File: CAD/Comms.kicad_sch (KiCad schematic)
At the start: 84 parts, among them J27 uSD_Socket, J43 USB, J46 ETHERNET, Q1 BC807, U13 MCP2542, U15 MCP2542, U16 KSZ8081RNACA, U17 74LVC2G125, U19 74LVC2G34, U3 EMIF06, U5 RClamp0504FB, U7 AP22816AKEWT, X2 25Mhz

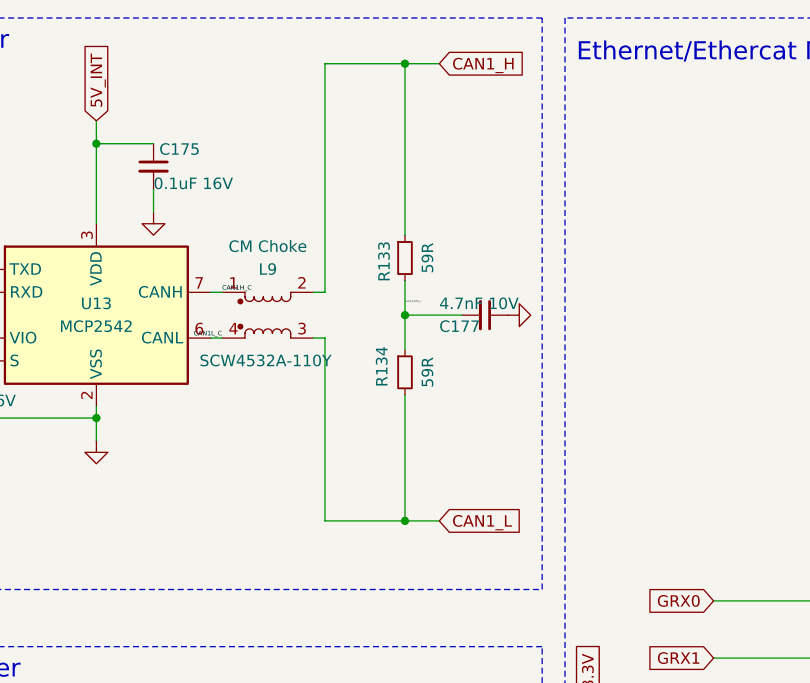
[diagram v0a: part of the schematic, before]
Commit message: OOPS, switched the symbols for psoitive and negative
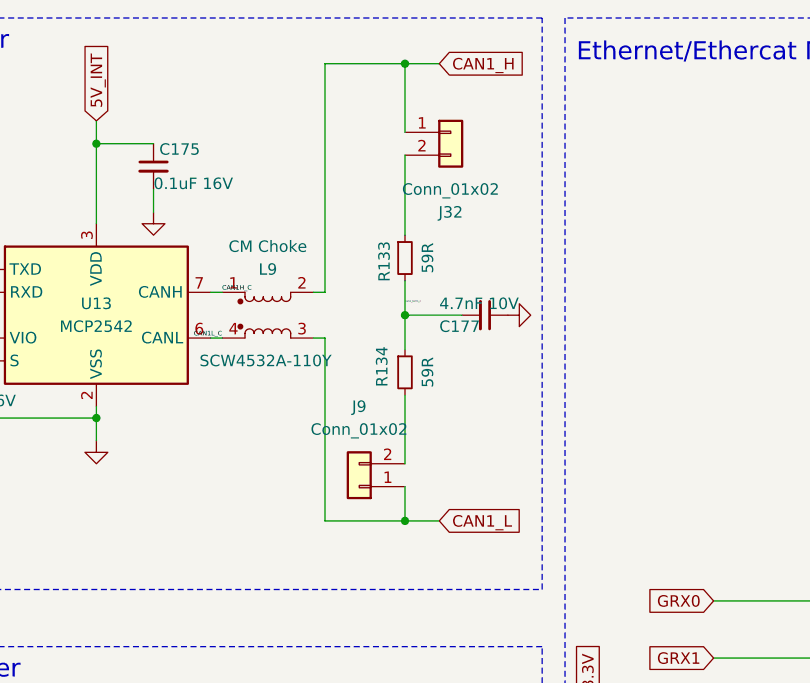
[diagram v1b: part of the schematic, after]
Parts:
- added J32, J9: Conn_01x02, Connector_PinHeader_2.54mm:PinHeader_1x02_P2.54mm_Vertical, symbol Connector_Generic:Conn_01x02
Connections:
- net CAN1_H: now also J32.1 (Pin_1); no longer R133.1
- net CAN1_L: now also J9.1 (Pin_1); no longer R134.2
- new net: J32.2 (Pin_2), R133.1
- new net: J9.2 (Pin_2), R134.2
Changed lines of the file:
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@@
 	(wire
 		(pts
+			(xy 86.36 67.31) (xy 86.36 71.12)
+		)
+		(stroke
+			(width 0)
+			(type default)
+		)
+	)
+	(wire
+		(pts
 			(xy 76.2 257.81) (xy 77.47 257.81)
 		)
@@
 	(wire
 		(pts
-			(xy 86.36 57.15) (xy 86.36 71.12)
+			(xy 86.36 57.15) (xy 86.36 64.77)
 		)
 		(stroke
@@
 	(wire
 		(pts
-			(xy 86.36 20.32) (xy 86.36 39.37)
+			(xy 86.36 20.32) (xy 86.36 27.94)
 		)
 		(stroke
@@
 	(wire
 		(pts
+			(xy 86.36 30.48) (xy 86.36 39.37)
+		)
+		(stroke
+			(width 0)
+			(type default)
+		)
+	)
+	(wire
+		(pts
 			(xy 90.17 170.18) (xy 93.98 170.18)
 		)
@@
 	)
 	(symbol
+		(lib_id "Connector_Generic:Conn_01x02")
+		(at 91.44 27.94 0)
+		(unit 1)
+		(exclude_from_sim no)
+		(in_bom yes)
+		(on_board yes)
+		(dnp no)
+		(fields_autoplaced yes)
+		(property "Reference" "J32"
+			(at 91.44 36.83 0)
+			(effects
+				(font
+					(size 1.27 1.27)
+				)
+			)
+		)
+		(property "Value" "Conn_01x02"
+			(at 91.44 34.29 0)
+			(effects
+				(font
+					(size 1.27 1.27)
+				)
+			)
+		)
+		(property "Footprint" "Connector_PinHeader_2.54mm:PinHeader_1x02_P2.54mm_Vertical"
+			(at 91.44 27.94 0)
+			(effects
+				(font
+					(size 1.27 1.27)
+				)
+				(hide yes)
+			)
+		)
+		(property "Datasheet" "~"
+			(at 91.44 27.94 0)
+			(effects
+				(font
+					(size 1.27 1.27)
+				)
+				(hide yes)
+			)
+		)
+		(property "Description" "Generic connector, single row, 01x02, script generated (kicad-library-utils/schlib/autogen/connector/)"
+			(at 91.44 27.94 0)
+			(effects
+				(font
+					(size 1.27 1.27)
+				)
+				(hide yes)
+			)
+		)
+		(property "LCSC" "C124375"
+			(at 91.44 27.94 0)
+			(effects
+				(font
+					(size 1.524 1.524)
+				)
+				(hide yes)
+			)
+		)
+		(property "RotOffset" "90"
+			(at 91.44 27.94 0)
+			(effects
+				(font
+					(size 1.524 1.524)
+				)
+				(hide yes)
+			)
+		)
+		(pin "1"
+		)
+		(pin "2"
+		)
+		(instances
+			(project "Duet3_MB_3DP"
+				(path "/94813053-1316-4754-9fb4-4dbbf7dc780d/00000000-0000-0000-0000-00005b64a4e7"
+					(reference "J32")
+					(unit 1)
+				)
+			)
+		)
+	)
+	(symbol
 		(lib_id "Device:R_Small")
 		(at 175.26 204.47 0)
@@
 					(unit 1)
 				)
+			)
+		)
+	)
+	(symbol
+		(lib_id "Connector_Generic:Conn_01x02")
+		(at 81.28 67.31 180)
+		(unit 1)
+		(exclude_from_sim no)
+		(in_bom yes)
+		(on_board yes)
+		(dnp no)
+		(fields_autoplaced yes)
+		(property "Reference" "J9"
+			(at 81.28 58.42 0)
+			(effects
+				(font
+					(size 1.27 1.27)
+				)
+			)
+		)
+		(property "Value" "Conn_01x02"
+			(at 81.28 60.96 0)
+			(effects
+				(font
+					(size 1.27 1.27)
+				)
+			)
+		)
+		(property "Footprint" "Connector_PinHeader_2.54mm:PinHeader_1x02_P2.54mm_Vertical"
+			(at 81.28 67.31 0)
+			(effects
+				(font
+					(size 1.27 1.27)
+				)
+				(hide yes)
+			)
+		)
+		(property "Datasheet" "~"
+			(at 81.28 67.31 0)
+			(effects
+				(font
+					(size 1.27 1.27)
+				)
+				(hide yes)
+			)
+		)
+		(property "Description" "Generic connector, single row, 01x02, script generated (kicad-library-utils/schlib/autogen/connector/)"
+			(at 81.28 67.31 0)
+			(effects
+				(font
+					(size 1.27 1.27)
+				)
+				(hide yes)
+			)
+		)
+		(property "LCSC" "C124375"
+			(at 81.28 67.31 0)
+			(effects
+				(font
+					(size 1.524 1.524)
+				)
+				(hide yes)
+			)
+		)
+		(property "RotOffset" "90"
+			(at 81.28 67.31 0)
+			(effects
+				(font
+					(size 1.524 1.524)
+				)
+				(hide yes)
+			)
+		)
+		(pin "1"
+		)
+		(pin "2"
+		)
+		(instances
+			(project "Duet3_MB_3DP"
+				(path "/94813053-1316-4754-9fb4-4dbbf7dc780d/00000000-0000-0000-0000-00005b64a4e7"
+					(reference "J9")
+					(unit 1)
+				)

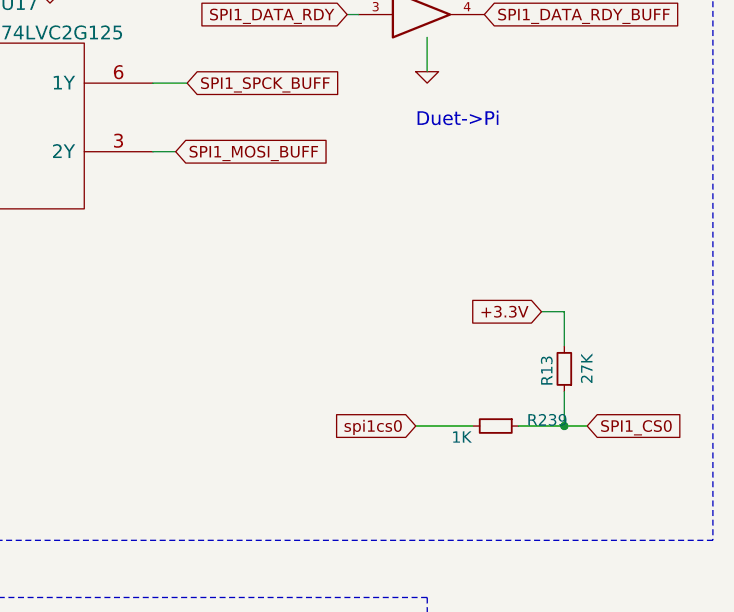
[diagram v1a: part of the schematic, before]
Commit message: Pin Changes / Misc
Changing some pins around so I have a chip select
Processor Pins:
PC28 ---> PA9 (Driver_2_Step)
PC29[AFE1_AD4] ---> PB1[AFE1_AD0] (TEMP_1)
PC28 -> spi1cs1
PC29 -> spi1cs2 (Unused as of now)
IDC Header:
CAN 0 Lines removed
13 -> SPI1_MOSI_BUFF
14 -> SP1_MISO
18 -> SPI1_SPCK_BUFF
19 -> spi1cs1
Misc:
Fixed all library links, should get a lot less errors now
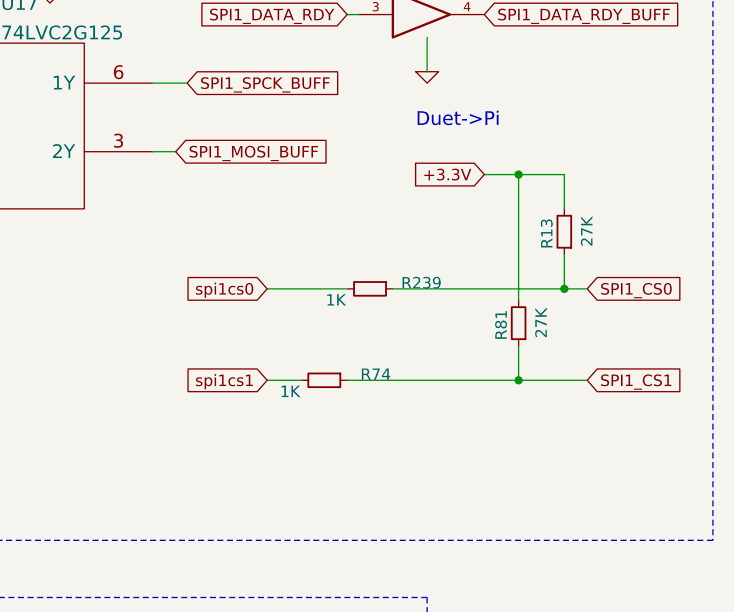
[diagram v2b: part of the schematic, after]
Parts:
- added R74: 1K, Resistor_SMD:R_0402_1005Metric, symbol Device:R_Small
- added R81: 27K, Resistor_SMD:R_0402_1005Metric, symbol Device:R_Small
- C14, C15, C171, C174, C175, C177, C181, C183, C188, C191, C192, C193, C194, C227: footprint Capacitor_SMD:C_0402_1005Metric_Wbry -> Capacitor_SMD:C_0402_1005Metric
- C184: footprint Capacitor_SMD:C_0603_1608Metric_Wbry -> Capacitor_SMD:C_0603_1608Metric
- L10: footprint Resistor_SMD:R_0603_1608Metric_Wbry -> Resistor_SMD:R_0603_1608Metric
- L9: footprint Carters_Various_Bits_and_Pieces:LineKey_CM_Choke_SCW_4532A -> 3DPotter:LineKey_CM_Choke_SCW_4532A
- R119, R122, R13, R130, R133, R134, R135, R136, R141, R142, R149, R150, R151, R174, R179, R188, R239, R66, R67, R70, R71, R75, R76, R77, R78, R80, R90: footprint Resistor_SMD:R_0402_1005Metric_Wbry -> Resistor_SMD:R_0402_1005Metric
- U16: footprint Carters_Various_Bits_and_Pieces:KSZ8081RNA _QFN-24-1EP_4x4mm_P0.5mm_EP2.6x2.6mm -> Package_DFN_QFN:QFN-24-1EP_4x4mm_P0.5mm_EP2.6x2.6mm
- U17: footprint Carters_Various_Bits_and_Pieces:X2-DFN2010-8 -> 3DPotter:X2-DFN2010-8
- U5: footprint complib:SC-70-6L -> 3DPotter:SC70_RCLAMP_SEM
- X2: footprint complib:Crystal_SMD_ECS-33B-4Pin_3.2x2.5mm -> Crystal:Crystal_SMD_3225-4Pin_3.2x2.5mm
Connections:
- net +3.3V: now also R81.2
- new net SPI1_CS1: R74.1, R81.1
- new net spi1cs1: R74.2
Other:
- moved on the sheet: R13, R239

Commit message: Board Finished
Board has been slightly modified to add SPI to the BBC.
A lot of library mismatch/ not found errors were fixed. Only errors that exist currently are all related to the silkscreen edges on all 0402 components.
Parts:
- U16: footprint Package_DFN_QFN:QFN-24-1EP_4x4mm_P0.5mm_EP2.6x2.6mm -> 3DPotter:QFN-24-1EP_4x4mm_P0.5mm_EP2.6x2.6mm_THT
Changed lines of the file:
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@@
 			)
 		)
-		(property "Footprint" "Package_DFN_QFN:QFN-24-1EP_4x4mm_P0.5mm_EP2.6x2.6mm"
+		(property "Footprint" "3DPotter:QFN-24-1EP_4x4mm_P0.5mm_EP2.6x2.6mm_THT"
 			(at 180.34 85.09 0)
 			(effects

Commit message: Update Revision 1.56
1.56 Should be production board that is going on all scara* and cartesian printers. 1.56 is a final check that everything is silkscreened properly and all connectors are the correct ones.
*Not all scaras. Only scara that does not have this board should be Jarret Gross' scara
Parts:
- U16: RotOffset 270 -> 180
- U19: RotOffset 270 -> 90
- U3: RotOffset 90 -> 270
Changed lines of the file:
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@@
 			)
 		)
-		(property "RotOffset" "270"
+		(property "RotOffset" "180"
 			(at 180.34 86.36 0)
 			(effects
@@
 			)
 		)
-		(property "RotOffset" "270"
+		(property "RotOffset" "90"
 			(at 251.46 181.61 0)
 			(effects
@@
 			)
 		)
-		(property "RotOffset" "270"
+		(property "RotOffset" "90"
 			(at 251.46 170.18 0)
 			(effects
@@
 			)
 		)
-		(property "RotOffset" "90"
+		(property "RotOffset" "270"
 			(at 69.85 177.8 0)
 			(effects

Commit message: Finalize changes for 1.56
LCSC and P/N updated for excessively out of stock parts.
Silkscreen changes so no more DRC errors
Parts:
- C14, C15, C17, C171, C174, C175, C177, C181, C183, C188, C191, C192, C193, C194, C227: footprint Capacitor_SMD:C_0402_1005Metric -> 3DPotter:0402_1005Metric_NoSilk
- R11, R119, R12, R122, R13, R130, R133, R134, R135, R136, R141, R142, R149, R150, R151, R174, R179, R188, R239, R5, R70, R71, R74, R75, R76, R77, R78, R80, R81, R90: footprint Resistor_SMD:R_0402_1005Metric -> 3DPotter:0402_1005Metric_NoSilk
- R66, R67: footprint Resistor_SMD:R_0402_1005Metric -> 3DPotter:0402_1005Metric_NoSilk; LCSC C226945 -> C2091853; Part Number AC0402FR-0728K7L -> AC0402FR-0728K7L(C226945) Alt CRCW040228K7FKED(C2091853)
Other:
- title: Duet 3 Main Board 3DP -> Duet 3 MB 3DP
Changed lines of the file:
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@@
 	(paper "A3" portrait)
 	(title_block
-		(title "Duet 3 Main Board 3DP")
-		(date "2026-02-17")
-		(rev "1.55")
+		(title "Duet 3 MB 3DP")
+		(date "2026-06-02")
+		(rev "1.56")
 		(company "3DPotter")
 		(comment 1 "(c) 3DPotter")
@@
 			)
 		)
-		(property "Footprint" "Resistor_SMD:R_0402_1005Metric"
+		(property "Footprint" "3DPotter:0402_1005Metric_NoSilk"
 			(at 67.31 220.98 0)
 			(effects
@@
 			)
 		)
-		(property "Footprint" "Resistor_SMD:R_0402_1005Metric"
+		(property "Footprint" "3DPotter:0402_1005Metric_NoSilk"
 			(at 59.69 224.79 0)
 			(effects
@@
 			)
 		)
-		(property "Footprint" "Resistor_SMD:R_0402_1005Metric"
+		(property "Footprint" "3DPotter:0402_1005Metric_NoSilk"
 			(at 48.26 228.6 0)
 			(effects
@@
 			)
 		)
-		(property "Footprint" "Capacitor_SMD:C_0402_1005Metric"
+		(property "Footprint" "3DPotter:0402_1005Metric_NoSilk"
 			(at 52.07 228.6 0)
 			(effects
@@
 			)
 		)
-		(property "Footprint" "Capacitor_SMD:C_0402_1005Metric"
+		(property "Footprint" "3DPotter:0402_1005Metric_NoSilk"
 			(at 58.42 31.75 0)
 			(effects
@@
 			)
 		)
-		(property "Footprint" "Capacitor_SMD:C_0402_1005Metric"
+		(property "Footprint" "3DPotter:0402_1005Metric_NoSilk"
 			(at 34.29 55.88 0)
 			(effects
@@
 			)
 		)
-		(property "Footprint" "Capacitor_SMD:C_0402_1005Metric"
+		(property "Footprint" "3DPotter:0402_1005Metric_NoSilk"
 			(at 95.25 48.26 0)
 			(effects
@@
 			)
 		)
-		(property "Footprint" "Resistor_SMD:R_0402_1005Metric"
+		(property "Footprint" "3DPotter:0402_1005Metric_NoSilk"
 			(at 86.36 41.91 0)
 			(effects
@@
 			)
 		)
-		(property "Footprint" "Resistor_SMD:R_0402_1005Metric"
+		(property "Footprint" "3DPotter:0402_1005Metric_NoSilk"
 			(at 86.36 54.61 0)
 			(effects
@@
 			)
 		)
-		(property "Footprint" "Resistor_SMD:R_0402_1005Metric"
+		(property "Footprint" "3DPotter:0402_1005Metric_NoSilk"
 			(at 128.27 96.52 0)
 			(effects
@@
 			)
 		)
-		(property "Footprint" "Resistor_SMD:R_0402_1005Metric"
+		(property "Footprint" "3DPotter:0402_1005Metric_NoSilk"
 			(at 148.59 73.66 0)
 			(effects
@@
 			)
 		)
-		(property "Footprint" "Resistor_SMD:R_0402_1005Metric"
+		(property "Footprint" "3DPotter:0402_1005Metric_NoSilk"
 			(at 130.81 115.57 0)
 			(effects
@@
 			)
 		)
-		(property "Footprint" "Capacitor_SMD:C_0402_1005Metric"
+		(property "Footprint" "3DPotter:0402_1005Metric_NoSilk"
 			(at 228.6 73.66 0)
 			(effects
@@
 			)
 		)
-		(property "Footprint" "Capacitor_SMD:C_0402_1005Metric"
+		(property "Footprint" "3DPotter:0402_1005Metric_NoSilk"
 			(at 228.6 81.28 0)
 			(effects
@@
 			)
 		)
-		(property "Footprint" "Resistor_SMD:R_0402_1005Metric"
+		(property "Footprint" "3DPotter:0402_1005Metric_NoSilk"
 			(at 222.25 87.63 0)
 			(effects
@@
 			)
 		)
-		(property "Footprint" "Resistor_SMD:R_0402_1005Metric"
+		(property "Footprint" "3DPotter:0402_1005Metric_NoSilk"
 			(at 220.98 92.71 0)
 			(effects
@@
 			)
 		)
-		(property "Footprint" "Resistor_SMD:R_0402_1005Metric"
+		(property "Footprint" "3DPotter:0402_1005Metric_NoSilk"
 			(at 201.93 110.49 0)
 			(effects
@@
 			)
 		)
-		(property "Footprint" "Capacitor_SMD:C_0402_1005Metric"
+		(property "Footprint" "3DPotter:0402_1005Metric_NoSilk"
 			(at 215.9 127 0)
 			(effects
@@
 			)
 		)
-		(property "Footprint" "Capacitor_SMD:C_0402_1005Metric"
+		(property "Footprint" "3DPotter:0402_1005Metric_NoSilk"
 			(at 240.03 127 0)
 			(effects
@@
 			)
 		)
-		(property "Footprint" "Resistor_SMD:R_0402_1005Metric"
+		(property "Footprint" "3DPotter:0402_1005Metric_NoSilk"
 			(at 123.19 100.33 0)
 			(effects
@@
 			)
 		)
-		(property "Footprint" "Resistor_SMD:R_0402_1005Metric"
+		(property "Footprint" "3DPotter:0402_1005Metric_NoSilk"
 			(at 152.4 58.42 0)
 			(effects
@@
 			)
 		)
-		(property "Footprint" "Resistor_SMD:R_0402_1005Metric"
+		(property "Footprint" "3DPotter:0402_1005Metric_NoSilk"
 			(at 237.49 101.6 0)
 			(effects
@@
 			)
 		)
-		(property "Footprint" "Resistor_SMD:R_0402_1005Metric"
+		(property "Footprint" "3DPotter:0402_1005Metric_NoSilk"
 			(at 158.75 118.11 0)
 			(effects
@@
 			)
 		)
-		(property "Footprint" "Capacitor_SMD:C_0402_1005Metric"
+		(property "Footprint" "3DPotter:0402_1005Metric_NoSilk"
 			(at 163.83 39.37 0)
 			(effects
@@
 			)
 		)
-		(property "Footprint" "Capacitor_SMD:C_0402_1005Metric"
+		(property "Footprint" "3DPotter:0402_1005Metric_NoSilk"
 			(at 170.18 41.91 0)
 			(effects
@@
 			)
 		)
-		(property "Footprint" "Capacitor_SMD:C_0402_1005Metric"
+		(property "Footprint" "3DPotter:0402_1005Metric_NoSilk"
 			(at 198.12 49.53 0)
 			(effects
@@
 			)
 		)
-		(property "Footprint" "Resistor_SMD:R_0402_1005Metric"
+		(property "Footprint" "3DPotter:0402_1005Metric_NoSilk"
 			(at 245.11 212.09 0)
 			(effects
@@
 			)
 		)
-		(property "Footprint" "Resistor_SMD:R_0402_1005Metric"
+		(property "Footprint" "3DPotter:0402_1005Metric_NoSilk"
 			(at 92.71 287.02 0)
 			(effects
@@
 			)
 		)
-		(property "Part Number" "AC0402FR-0728K7L"
+		(property "Part Number" "AC0402FR-0728K7L(C226945) Alt CRCW040228K7FKED(C2091853)"
 			(at 92.71 287.02 0)
 			(effects
@@
 			)
 		)
-		(property "LCSC" "C226945"
+		(property "LCSC" "C2091853"
 			(at 92.71 287.02 90)
 			(effects
@@
 			)
 		)
-		(property "Footprint" "Resistor_SMD:R_0402_1005Metric"
+		(property "Footprint" "3DPotter:0402_1005Metric_NoSilk"
 			(at 85.09 287.02 0)
 			(effects
@@
 			)
 		)
-		(property "Part Number" "AC0402FR-0728K7L"
+		(property "Part Number" "AC0402FR-0728K7L(C226945) Alt CRCW040228K7FKED(C2091853)"
 			(at 85.09 287.02 0)
 			(effects
@@
 			)
 		)
-		(property "LCSC" "C226945"
+		(property "LCSC" "C2091853"
 			(at 85.09 287.02 90)
 			(effects
@@
 			)
 		)
-		(property "Footprint" "Resistor_SMD:R_0402_1005Metric"
+		(property "Footprint" "3DPotter:0402_1005Metric_NoSilk"
 			(at 266.7 205.74 0)
 			(effects
@@
 			)
 		)
-		(property "Footprint" "Resistor_SMD:R_0402_1005Metric"
+		(property "Footprint" "3DPotter:0402_1005Metric_NoSilk"
 			(at 78.74 306.07 0)
 			(effects
@@
 			)
 		)
-		(property "Footprint" "Capacitor_SMD:C_0402_1005Metric"
+		(property "Footprint" "3DPotter:0402_1005Metric_NoSilk"
 			(at 209.55 172.72 0)
 			(effects
@@
 			)
 		)
-		(property "Footprint" "Resistor_SMD:R_0402_1005Metric"
+		(property "Footprint" "3DPotter:0402_1005Metric_NoSilk"
 			(at 181.61 204.47 0)
 			(effects
@@
 			)
 		)
-		(property "Footprint" "Resistor_SMD:R_0402_1005Metric"
+		(property "Footprint" "3DPotter:0402_1005Metric_NoSilk"
 			(at 54.61 302.26 0)
 			(effects
@@
 			)
 		)
-		(property "Footprint" "Resistor_SMD:R_0402_1005Metric"
+		(property "Footprint" "3DPotter:0402_1005Metric_NoSilk"
 			(at 175.26 204.47 0)
 			(effects
@@
 			)
 		)
-		(property "Footprint" "Resistor_SMD:R_0402_1005Metric"
+		(property "Footprint" "3DPotter:0402_1005Metric_NoSilk"
 			(at 48.26 341.63 0)
 			(effects
@@
 			)
 		)
-		(property "Footprint" "Resistor_SMD:R_0402_1005Metric"
+		(property "Footprint" "3DPotter:0402_1005Metric_NoSilk"
 			(at 85.09 279.4 0)
 			(effects
@@
 			)
 		)
-		(property "Footprint" "Capacitor_SMD:C_0402_1005Metric"
+		(property "Footprint" "3DPotter:0402_1005Metric_NoSilk"
 			(at 53.34 326.39 0)
 			(effects
@@
 			)
 		)
-		(property "Footprint" "Resistor_SMD:R_0402_1005Metric"
+		(property "Footprint" "3DPotter:0402_1005Metric_NoSilk"
 			(at 85.09 326.39 0)
 			(effects
@@
 			)
 		)
-		(property "Footprint" "Capacitor_SMD:C_0402_1005Metric"
+		(property "Footprint" "3DPotter:0402_1005Metric_NoSilk"
 			(at 259.08 160.02 0)
 			(effects
@@
 			)
 		)
-		(property "Footprint" "Resistor_SMD:R_0402_1005Metric"
+		(property "Footprint" "3DPotter:0402_1005Metric_NoSilk"
 			(at 261.62 215.9 0)
 			(effects
@@
 			)
 		)
-		(property "Footprint" "Resistor_SMD:R_0402_1005Metric"
+		(property "Footprint" "3DPotter:0402_1005Metric_NoSilk"
 			(at 99.06 168.91 0)
 			(effects
@@
 			)
 		)
-		(property "Footprint" "Resistor_SMD:R_0402_1005Metric"
+		(property "Footprint" "3DPotter:0402_1005Metric_NoSilk"
 			(at 107.95 334.01 0)
 			(effects
@@
 			)
 		)
-		(property "Footprint" "Resistor_SMD:R_0402_1005Metric"
+		(property "Footprint" "3DPotter:0402_1005Metric_NoSilk"
 			(at 78.74 290.83 0)
 			(effects
@@
 			)
 		)
-		(property "Footprint" "Resistor_SMD:R_0402_1005Metric"
+		(property "Footprint" "3DPotter:0402_1005Metric_NoSilk"
 			(at 240.03 222.25 0)
 			(effects
@@
 			)
 		)
-		(property "Footprint" "Capacitor_SMD:C_0402_1005Metric"
+		(property "Footprint" "3DPotter:0402_1005Metric_NoSilk"
 			(at 93.98 334.01 0)
 			(effects
@@
 			)
 		)
-		(property "Footprint" "Resistor_SMD:R_0402_1005Metric"
+		(property "Footprint" "3DPotter:0402_1005Metric_NoSilk"
 			(at 63.5 308.61 0)
 			(effects
